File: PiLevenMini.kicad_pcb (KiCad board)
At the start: 2 copper layers, 56 x 65 mm, 143 parts, among them IC1 ATMEGA328P-A, J1 RASPBERRY_PI_PLUS_CON, Q1 RJU003N03, Q10 RJU003N03, Q11 RJU003N03, Q2 RJU003N03, Q6 RJU003N03, Q7 BSS84, Q8 BSS84, Q9 RJU003N03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

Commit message: V1.0
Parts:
- removed the 1pin_prototyping at (147.3, 135.9)
- removed the 1pin_prototyping at (147.3, 133.3)
- removed the 1pin_prototyping at (147.3, 130.8)
- added 1pin_prototyping: val**, FT:1pin_prototyping, F.Cu at (152.4, 115.6)
- added 1pin_prototyping: val**, FT:1pin_prototyping, F.Cu at (154.9, 113.0)
- added 1pin_prototyping: val**, FT:1pin_prototyping, F.Cu at (152.4, 113.0)
- moved SJ7 1.84 mm to (135.4, 127.0)
- moved C10 1.49 mm to (132.5, 103.1)
- moved C11 1.41 mm to (133.4, 102.1)
- moved SJ2 1.04 mm to (135.3, 130.8)
- moved SJ3 0.34 mm to (135.3, 134.5)
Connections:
- 1pin_prototyping pad 1: (no net) -> GND (x11)
- 1pin_prototyping pad 1: (no net) -> +5V (x6)
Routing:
- net GND: track 172.0 -> 246.6 mm, vias 39 -> 41
- net +5V: track 255.5 -> 280.5 mm
- net /EXT_CTS: track 49.8 -> 60.0 mm
- net /CTS_5V: track 11.8 -> 16.6 mm
- net Net-(Q1-PadD): track 8.40 -> 11.0 mm
- net /D11_MOSI: track 79.0 -> 81.3 mm
- net /D7: track 35.7 -> 33.7 mm
- net /D6: track 36.3 -> 34.5 mm
- net /D5: track 33.2 -> 31.4 mm
- net /AVR_RX: track 75.0 -> 73.5 mm
- net /D4: track 27.9 -> 26.5 mm
- net Net-(C11-Pad1): track 12.4 -> 13.5 mm
- net Net-(C10-Pad1): track 10.6 -> 11.6 mm
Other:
- board text added: "10"
- board text added: "11"
- board text added: "12"
- board text added: "13"
- board text added: "3V3"
- board text added: "5V"
- board text added: "9"
- board text added: "A REF"
- board text added: "A0"
- board text added: "A1"
- board text added: "A2"
- board text added: "A3"
- board text added: "A4"
- board text added: "A5"
- board text added: "AVR RX"
- board text added: "AVR TX"
- board text added: "CTS/RESET"
- board text added: "FTDI CTS /RESET"
- board text added: "FTDI VOUT /5V"
- board text added: "GREEN"
- board text added: "IO Ref"
- board text added: "NC"
- board text added: "RST"
- board text added: "SCL"
- board text added: "SDA"
- board text added: "SKU: PILVM Designed by Angus Gratton"
- board text added: "VIN"
- board text added: "tron.cc/pilvmini"
- board text added: "www.freetronics.com"
- board text removed: "YELLOW"

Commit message: Cleanup silk, place serial connector on-grid
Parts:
- moved SJ1 0.54 mm to (151.1, 92.7)
- moved SJ6 0.42 mm to (143.5, 92.7)
- moved JP1 0.30 mm to (138.4, 89.5)
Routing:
- net +5V: track 280.5 -> 282.5 mm

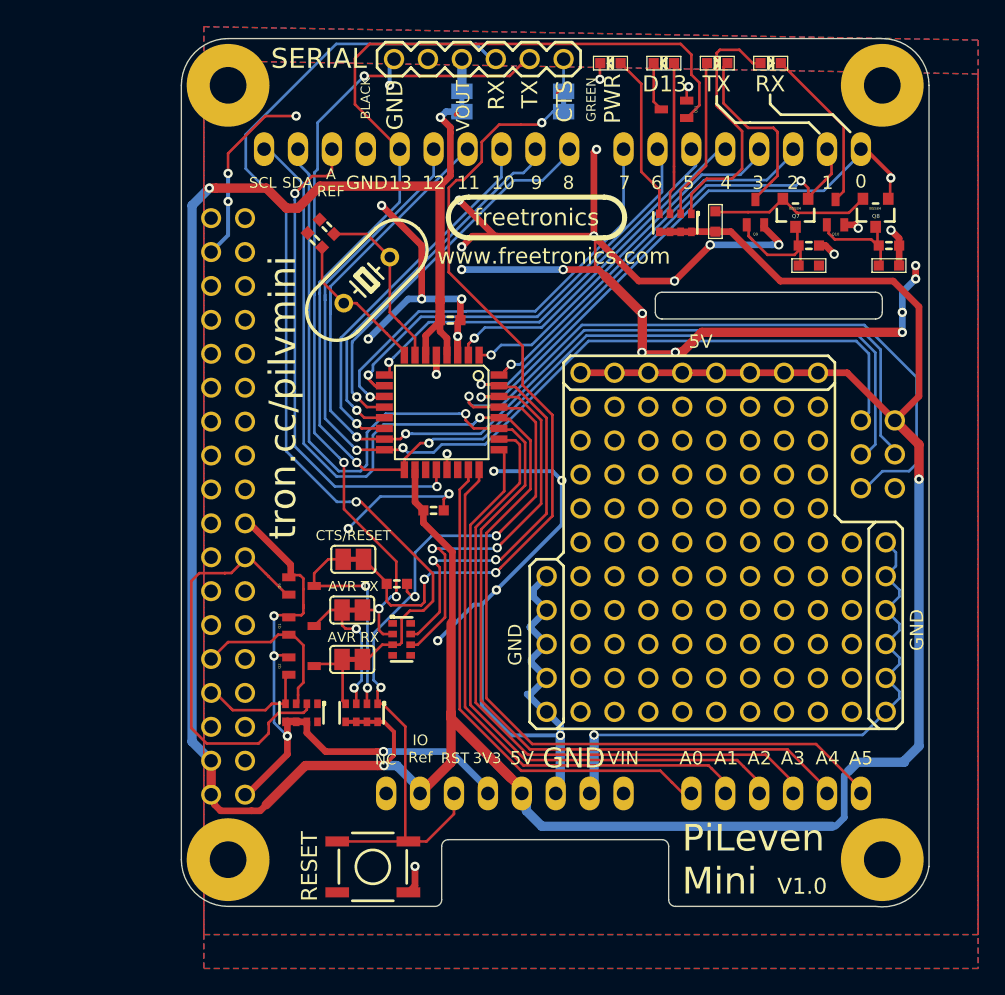
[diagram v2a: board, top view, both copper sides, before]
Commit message: V1.1: Fix V1.0 pin assignment problem, minor cleanup
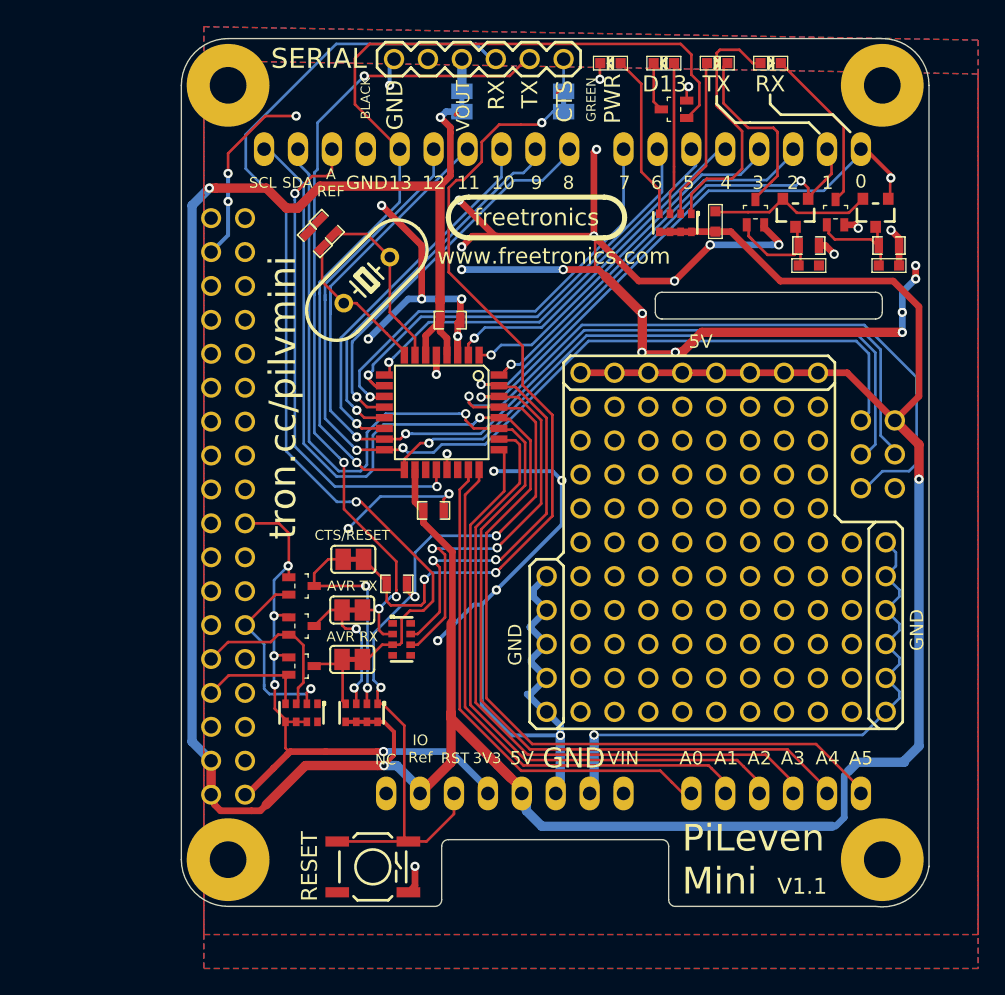
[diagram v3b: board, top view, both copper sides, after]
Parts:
- C10, C11, C12, C13, C14, C16, C9: footprint FT:CAP0603 -> FT:0603_CAP
- IC1: footprint FT:TQFP32-08 -> FT:QFP32_7mm_0.8mm
- Q1, Q10, Q11, Q2, Q6, Q9: footprint FT:SOT323_MOSFET -> FT:SOT323_FET
- Q7, Q8: footprint FT:SOT23_MOSFET -> FT:SOT23_FET
- SHIELD1: value ARDUINO_SHIELD -> ARDUINO_FOOTPRINT
- SW1: value PUSHBUTTON -> SW_PUSHBUTTON; footprint FT:TACTILE_SWITCH_SMD -> FT:SW_PUSHBUTTON_SMD
- X1: footprint FT:HC49-US -> FT:CRYSTAL_HC49_PTH
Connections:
- J1 pad 11: (no net) -> /PI_RTS
- J1 pad 15: /PI_RTS -> (no net)
- SW1 pad 2: /AVR_RESET -> GND
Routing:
- net /PI_RTS: track 31.5 -> 15.1 mm, vias 0 -> 1
- net +3.3V: track 47.8 -> 46.9 mm, vias 4 -> 5
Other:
- board text added: "V1.1"
- board text removed: "V1.0"

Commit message: Minor board cleanup for 1.1 release
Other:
- board text added: "Copyright (C) 2015 Freetronics Pty Ltd TAPR Open Hardware License http://tapr.org/ohl"
- board text removed: "Copyright (C) 2014 Freetronics Pty Ltd TAPR Open Hardware License http://tapr.org/ohl"
